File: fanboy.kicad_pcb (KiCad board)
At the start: 6 copper layers, 0 parts

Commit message: finished routing, added render and readme
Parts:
- added C100: 0.1uF, Capacitor_SMD:C_0402_1005Metric, F.Cu at (175.3, 73.5)
- added C101: 0.1uF, Capacitor_SMD:C_0402_1005Metric, F.Cu at (181.2, 74.0)
- added C102: 1uF, Capacitor_SMD:C_0402_1005Metric, F.Cu at (180.6, 88.0)
- added C103: 1uF, Capacitor_SMD:C_0402_1005Metric, F.Cu at (183.0, 80.7)
- added C104: 0.1uF, Capacitor_SMD:C_0402_1005Metric, F.Cu at (182.9, 76.6)
- added C105: 0.1uF, Capacitor_SMD:C_0402_1005Metric, F.Cu at (180.9, 85.7)
- added C106: 0.1uF, Capacitor_SMD:C_0402_1005Metric, F.Cu at (182.3, 85.6)
- added C107: 0.1uF, Capacitor_SMD:C_0402_1005Metric, F.Cu at (171.3, 80.3)
- added C108: 0.1uF, Capacitor_SMD:C_0402_1005Metric, F.Cu at (182.3, 75.1)
- added C109: 0.1uF, Capacitor_SMD:C_0402_1005Metric, F.Cu at (172.1, 76.8)
- added C110: 0.1uF, Capacitor_SMD:C_0402_1005Metric, F.Cu at (175.3, 72.5)
- added C14: 220uF, Capacitor_SMD:CP_Elec_6.3x7.7, F.Cu at (159.1, 94.1)
- added C19: 220uF, Capacitor_SMD:CP_Elec_6.3x7.7, F.Cu at (179.3, 94.2)
- added C20: 311-3342-1-ND, Capacitor_SMD:C_0402_1005Metric, F.Cu at (178.5, 98.8)
- added C21: 311-3342-1-ND, Capacitor_SMD:C_0402_1005Metric, F.Cu at (157.7, 98.8)
- added C6: 311-3342-1-ND, Capacitor_SMD:C_0402_1005Metric, F.Cu at (165.5, 93.7)
- added C90: 1uF, Capacitor_SMD:C_0402_1005Metric, F.Cu at (182.9, 73.4)
- added C96: 30pF, Capacitor_SMD:C_0402_1005Metric, F.Cu at (179.1, 88.0)
- added C97: 30pF, Capacitor_SMD:C_0402_1005Metric, F.Cu at (174.4, 86.9)
- added C98: 1uF, Capacitor_SMD:C_0402_1005Metric, F.Cu at (193.6, 75.9)
- added C99: 0.1uF, Capacitor_SMD:C_0402_1005Metric, F.Cu at (173.0, 72.3)
- added G***: LOGO, bitaxe:fanboy_logo, F.Cu at (155.6, 83.0)
- added J1: XT30, bitaxe:XT30PW-M, F.Cu at (150.5, 73.5)
- added J3: Conn_01x04, bitaxe:470531000, F.Cu at (158.5, 103.0)
- added J4: Conn_01x04, bitaxe:470531000, F.Cu at (179.3, 103.4)
- added J6: USB_C_Receptacle_USB2.0, aditBoard:USB_C_Receptacle_GCT_USB4105-xx-A_16P_TopMnt_Horizontal, F.Cu at (177.4, 65.1)
- added R10: 5.6k, Resistor_SMD:R_0402_1005Metric, F.Cu at (160.2, 98.8)
- added R13: 5.6k, Resistor_SMD:R_0402_1005Metric, F.Cu at (181.1, 98.8)
- added R19: 4.7k, Resistor_SMD:R_0402_1005Metric, F.Cu at (170.4, 89.7)
- added R20: 4.7k, Resistor_SMD:R_0402_1005Metric, F.Cu at (172.2, 89.7)
- added R34: 49.9k, Resistor_SMD:R_0402_1005Metric, F.Cu at (165.3, 72.8)
- added R50: 10k, Resistor_SMD:R_0402_1005Metric, F.Cu at (168.1, 72.8)
- added R51: 5.1k, Resistor_SMD:R_0402_1005Metric, F.Cu at (183.7, 66.1)
- added R52: 5.1k, Resistor_SMD:R_0402_1005Metric, F.Cu at (171.3, 66.1)
- added R53: 33, Resistor_SMD:R_0402_1005Metric, F.Cu at (178.0, 73.0)
- added R54: 33, Resistor_SMD:R_0402_1005Metric, F.Cu at (179.1, 73.0)
- added R55: 1k, Resistor_SMD:R_0402_1005Metric, F.Cu at (166.7, 72.8)
- added R6: 10k, Resistor_SMD:R_0402_1005Metric, F.Cu at (183.7, 98.8)
- added R9: 10k, Resistor_SMD:R_0402_1005Metric, F.Cu at (162.9, 98.8)
- added SW1: GT-TC029B-H025-L1N, bitaxe:SW_CS1213AGF260_CRS, F.Cu at (167.7, 68.7)
- added SW2: GT-TC029B-H025-L1N, bitaxe:SW_CS1213AGF260_CRS, F.Cu at (160.8, 68.7)
- added TP1: TestPoint, TestPoint:TestPoint_Pad_D1.0mm, F.Cu at (172.0, 87.5)
- added TP2: TestPoint, TestPoint:TestPoint_Pad_D1.0mm, F.Cu at (171.3, 84.6)
- added TP3: TestPoint, TestPoint:TestPoint_Pad_D1.0mm, F.Cu at (169.4, 86.8)
- added U10: TLV1117LV33DCYR, emberone:VREG_TLV1117LV33DCYR, F.Cu at (189.4, 76.8)
- added U27: RP2040, Package_DFN_QFN:QFN-56-1EP_7x7mm_P0.4mm_EP3.2x3.2mm, F.Cu at (177.6, 79.7)
- added U5: EMC2302, Package_SO:MSOP-10_3x3mm_P0.5mm, F.Cu at (169.6, 93.4)
- added U8: W25Q16JVUXIQ TR, emberone:USON-8_UX_2x3x0p6_WIN, F.Cu at (171.2, 74.3)
- added U9: SK6812, emberone:LED-SMD_4P-L4.0-W1.6-L, F.Cu at (188.1, 63.3)
- added Y1: 12MHz, emberone:XTAL_ECS-120-20-33-CKM-TR3, F.Cu at (176.7, 86.9)
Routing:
- net /3V3: track 0.00 -> 50.1 mm, vias 0 -> 20
- net Net-(U27-GPIO1): track 0.00 -> 42.5 mm, vias 0 -> 2
- net Net-(U27-RUN): track 0.00 -> 29.3 mm, vias 0 -> 2
- net /1V1: track 0.00 -> 26.2 mm, vias 0 -> 3
- net /FAN2_PWM: track 0.00 -> 19.0 mm
- net /SWCLK: track 0.00 -> 17.4 mm, vias 0 -> 2
- net /SCL: track 0.00 -> 17.0 mm
- net /FAN2_TACH: track 0.00 -> 16.4 mm, vias 0 -> 2
- net /FAN1_TACH: track 0.00 -> 16.3 mm
- net /SDA: track 0.00 -> 16.3 mm
- net /SWD: track 0.00 -> 16.0 mm, vias 0 -> 2
- net /QSPI_SS: track 0.00 -> 13.7 mm, vias 0 -> 2
- net /FAN1_PWM: track 0.00 -> 12.3 mm, vias 0 -> 2
- net /QSPI_SD1: track 0.00 -> 12.2 mm, vias 0 -> 2
- net /QSPI_SD2: track 0.00 -> 10.9 mm, vias 0 -> 2
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- added copper zone on In2.Cu, net /12V
- added copper zone on F.Cu, net /3V3
- added copper zone on In2.Cu, net /3V3
- added copper zone on B.Cu, net /5V
- added copper zone on F.Cu, net /5V
- added copper zone on In3.Cu, net /5V
- added copper zone on F.Cu, net GND
- added copper zone on In1.Cu, net GND
- added copper zone on In4.Cu, net GND
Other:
- board outline added: 52.8 x 46.8 mm
- board text added: "BOOT"
- board text added: "FAN #1"
- board text added: "FAN #2"
- board text added: "LFG"
- board text added: "RESET"
- board text added: "v1"

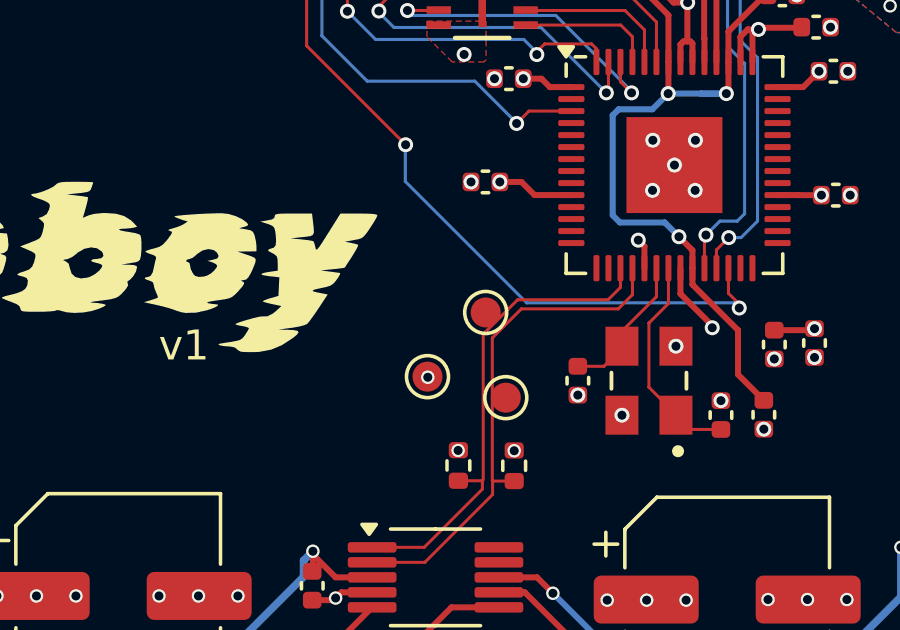
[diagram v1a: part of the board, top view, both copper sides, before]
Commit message: added BOM
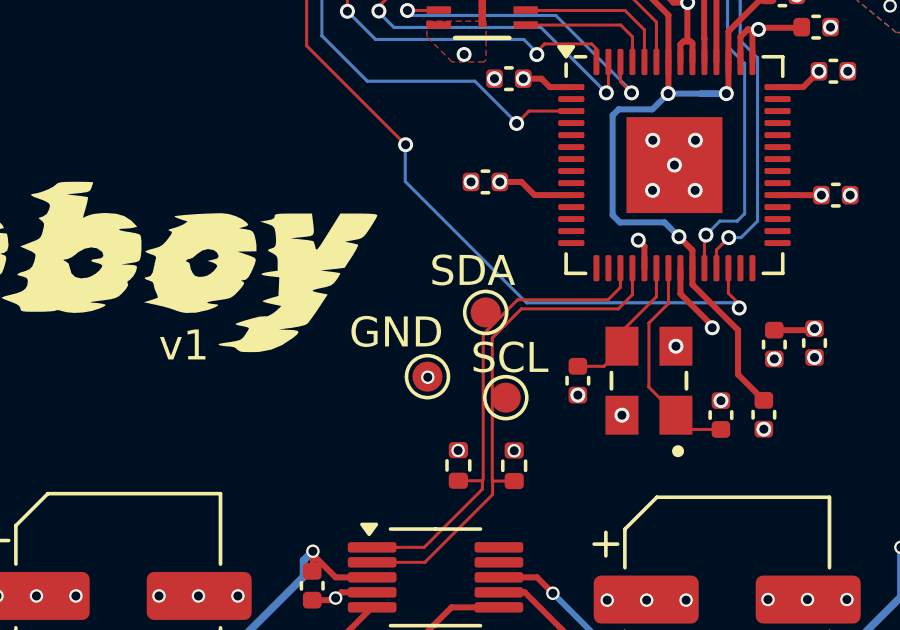
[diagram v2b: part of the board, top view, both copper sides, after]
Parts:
- TP1: value TestPoint -> SCL
- TP2: value TestPoint -> SDA
- TP3: value TestPoint -> GND
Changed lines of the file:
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@@
 			)
 		)
-		(property "Value" "TestPoint"
-			(at 0 1.55 180)
-			(layer "F.Fab")
+		(property "Value" "SCL"
+			(at -0.13 1.32 180)
+			(layer "F.SilkS")
 			(effects
 				(font
@@
 			)
 		)
-		(property "Value" "TestPoint"
-			(at 0 1.55 180)
-			(layer "F.Fab")
+		(property "Value" "SDA"
+			(at 0.44 1.38 180)
+			(layer "F.SilkS")
 			(effects
 				(font
@@
 			)
 		)
-		(property "Value" "TestPoint"
-			(at 0 1.55 0)
-			(layer "F.Fab")
+		(property "Value" "GND"
+			(at -1.04 -1.47 0)
+			(layer "F.SilkS")
 			(effects
 				(font

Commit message: connect FAN_ALERT to EMC2103 and add pullup
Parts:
- added R1: 10k, Resistor_SMD:R_0402_1005Metric, F.Cu at (173.8, 90.2)
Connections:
- U27 pad 4: /THERM -> /FAN_ALERT
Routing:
- net /FAN_ALERT: track 0.00 -> 16.1 mm, vias 0 -> 2
- net Net-(U27-RUN): track 29.3 -> 28.6 mm
- net /3V3: vias 20 -> 21

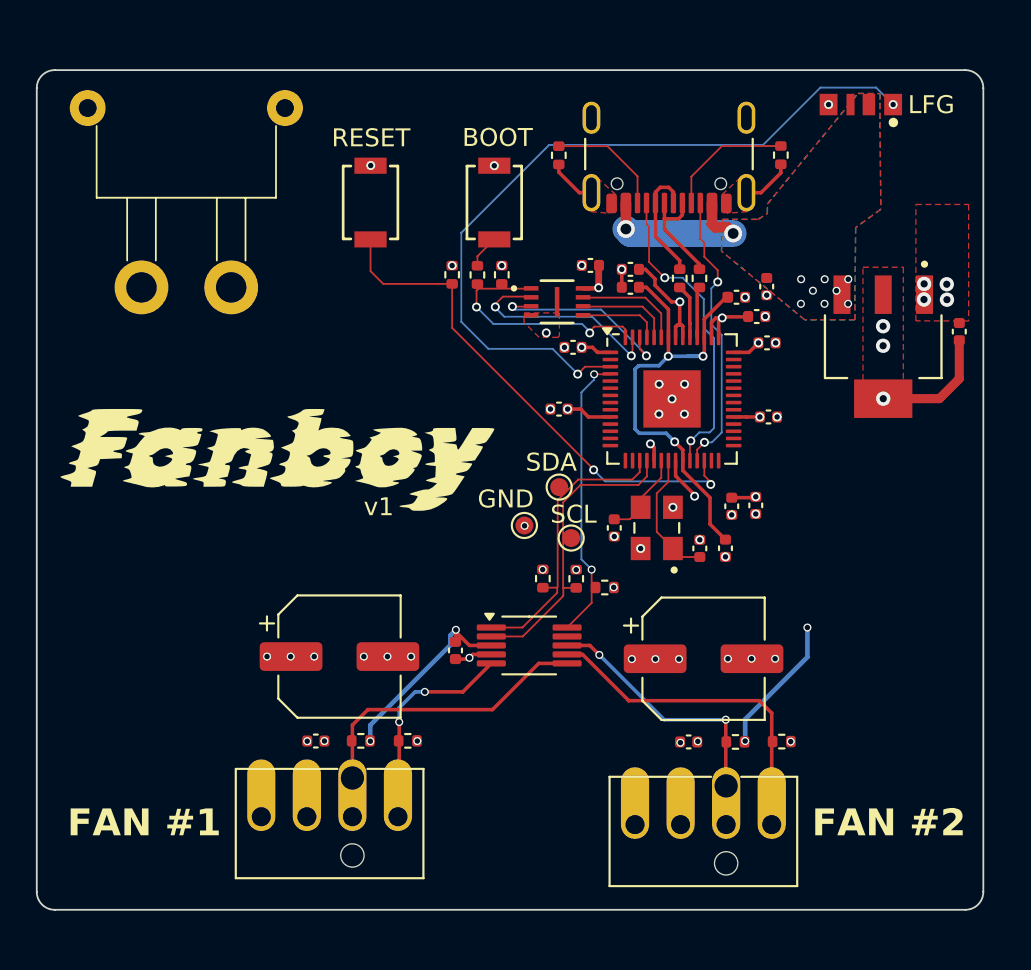
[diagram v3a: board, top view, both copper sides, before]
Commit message: moved schematic symbols into separate library. added checked gerbers
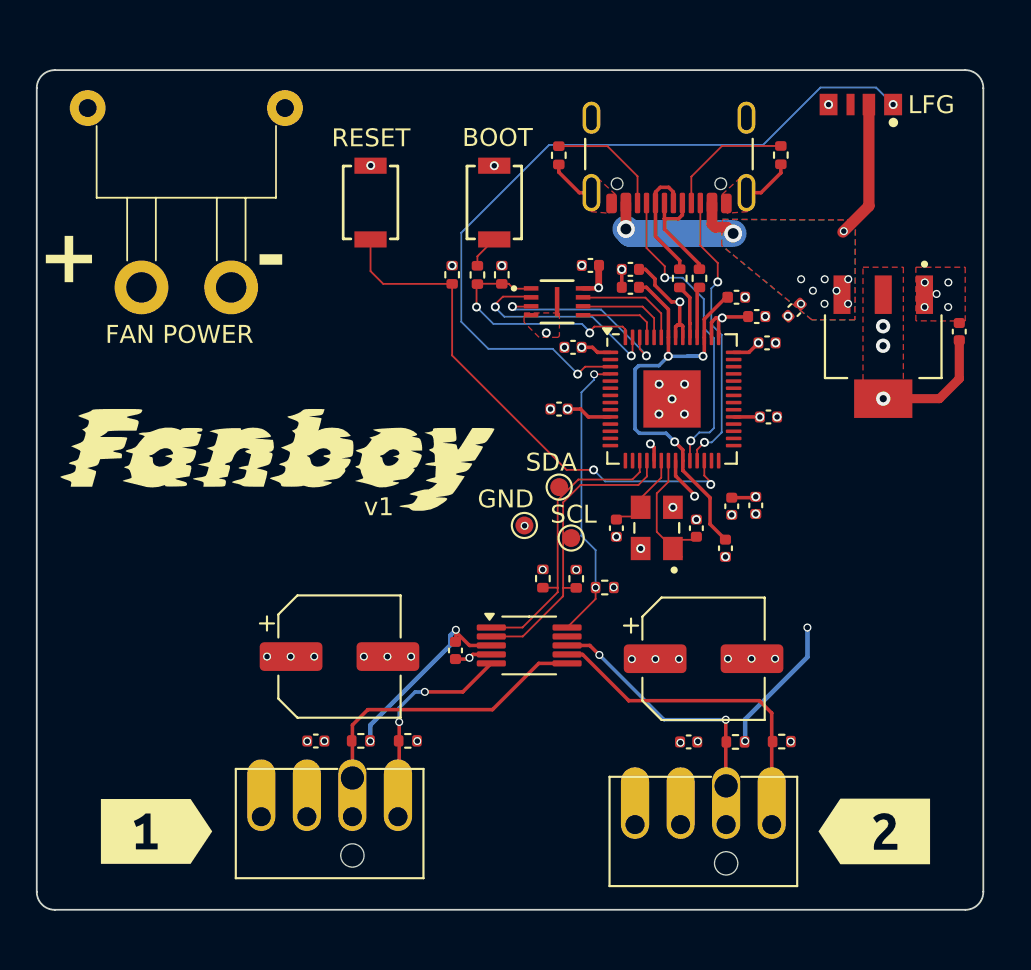
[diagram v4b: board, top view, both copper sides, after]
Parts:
- added kibuzzard-68D55084: G***, kibuzzard-68D55084, F.Cu at (148.8, 103.8)
- added kibuzzard-68D55096: G***, kibuzzard-68D55096, F.Cu at (188.9, 103.8)
- moved C90 2.02 mm to (184.4, 74.7), turned to -135 degrees
- moved C96 1.15 mm to (178.9, 86.9)
- moved C97 0.12 mm to (174.5, 86.9)
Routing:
- net /5V: track 10.1 -> 17.9 mm, vias 12 -> 13
- net /XOUT: track 7.22 -> 8.14 mm
- net Net-(U27-RUN): track 28.6 -> 29.5 mm
- net GND: vias 40 -> 41
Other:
- board text added: "+"
- board text added: "-"
- board text added: "FAN POWER"
- board text removed: "FAN #1"
- board text removed: "FAN #2"

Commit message: added mounting holes and fiducials. made board even 50x50mm. generated and checked gerbers
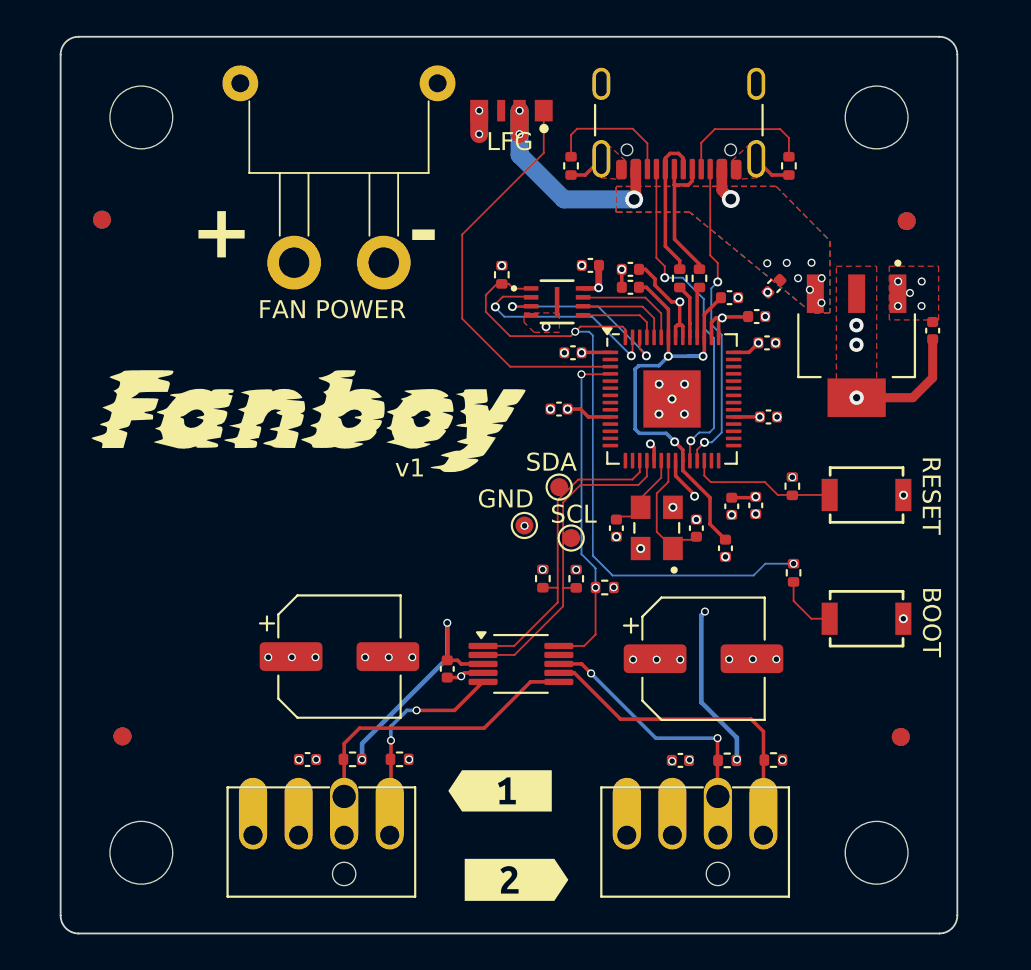
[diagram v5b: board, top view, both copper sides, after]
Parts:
- removed kibuzzard-68D55084: G***, kibuzzard-68D55084
- removed kibuzzard-68D55096: G***, kibuzzard-68D55096
- added FID1: Fiducial, bitaxe:Fiducial_1mm_Mask2mm, F.Cu at (145.8, 69.7)
- added FID2: Fiducial, bitaxe:Fiducial_1mm_Mask2mm, F.Cu at (146.9, 98.5)
- added FID3: Fiducial, bitaxe:Fiducial_1mm_Mask2mm, F.Cu at (190.3, 98.5)
- added FID4: Fiducial, bitaxe:Fiducial_1mm_Mask2mm, F.Cu at (190.7, 69.8)
- added H1: MountingHole, MountingHole:MountingHole_3.5mm, F.Cu at (148.0, 64.0)
- added H2: MountingHole, MountingHole:MountingHole_3.5mm, F.Cu at (148.0, 105.0)
- added H3: MountingHole, MountingHole:MountingHole_3.5mm, F.Cu at (189.0, 105.0)
- added H4: MountingHole, MountingHole:MountingHole_3.5mm, F.Cu at (189.0, 64.0)
- added kibuzzard-68D56264: G***, kibuzzard-68D56264, F.Cu at (168.0, 101.5)
- added kibuzzard-68D5627E: G***, kibuzzard-68D5627E, F.Cu at (168.9, 106.5)
- moved SW2 32.1 mm to (188.4, 85.0), turned to 0 degrees
- moved SW1 31.1 mm to (188.4, 92.0), turned to 0 degrees
- moved R55 24.2 mm to (184.4, 89.4), turned to -90 degrees
- moved R34 22.3 mm to (184.3, 84.6)
- moved U9 19.5 mm to (168.6, 63.6)
- moved J1 8.62 mm to (159.0, 72.1)
- moved G*** 2.77 mm to (157.3, 80.8)
- moved J6 1.97 mm to (178.0, 63.2)
- moved C90 1.75 mm to (183.3, 73.4)
- moved C98 1.49 mm to (192.1, 75.9)
- moved U10 1.49 mm to (187.9, 76.7)
- moved C20 1.13 mm to (178.1, 99.8)
- moved C6 1.13 mm to (165.1, 94.8)
- moved J3 1.13 mm to (158.0, 104.0)
- moved R10 1.13 mm to (159.8, 99.8)
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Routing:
- net /QSPI_SS: track 14.1 -> 38.2 mm
- net Net-(U27-RUN): track 29.5 -> 8.27 mm, vias 2 -> 0
- net Net-(U27-GPIO1): track 42.5 -> 22.9 mm, vias 2 -> 0
- net /3V3: track 50.1 -> 53.9 mm
- net /5V: track 17.9 -> 14.8 mm
- net /FAN_ALERT: track 16.3 -> 18.8 mm
- net /USB_DP: track 7.78 -> 9.45 mm
- net /SWD: track 16.0 -> 17.7 mm
- net /SWCLK: track 17.4 -> 19.1 mm
- net /USB_DN: track 6.09 -> 7.75 mm
- net Net-(R55-Pad2): track 1.86 -> 3.48 mm
- net /SCL: track 17.0 -> 18.3 mm
- net /SDA: track 16.3 -> 17.6 mm
- net Net-(J6-CC2): track 6.58 -> 7.39 mm
- net Net-(J6-CC1): track 7.17 -> 7.93 mm
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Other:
- board size 52.8 x 46.8 mm -> 50 x 50 mm
